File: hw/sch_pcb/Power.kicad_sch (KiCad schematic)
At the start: 20 parts, among them U1 NCP1117ST33, U11 TPS563249

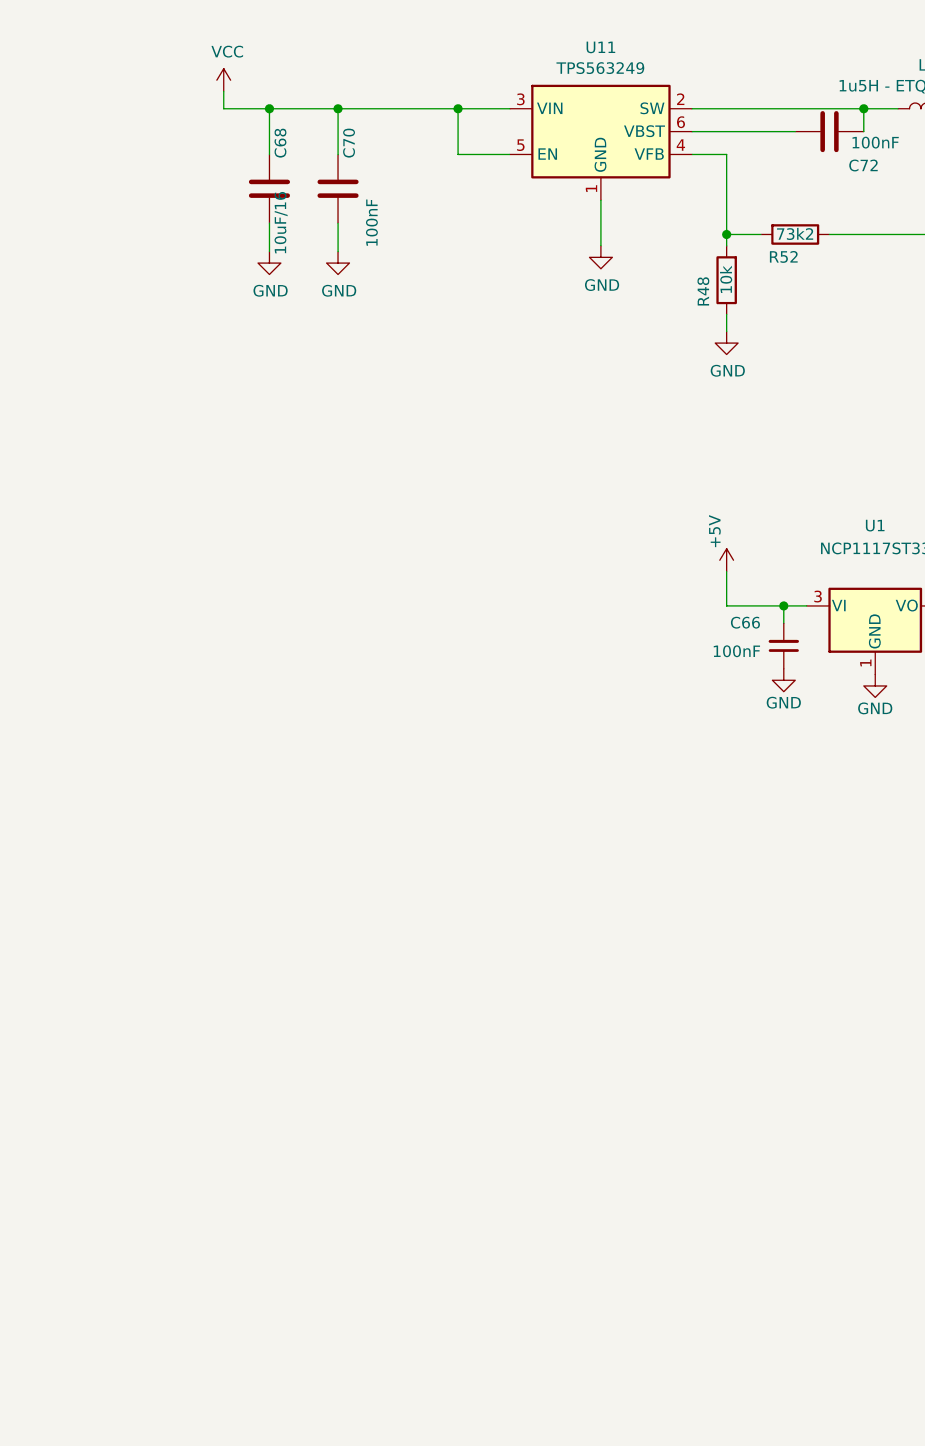
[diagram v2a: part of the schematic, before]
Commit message: Add thermistor #22, align text labels
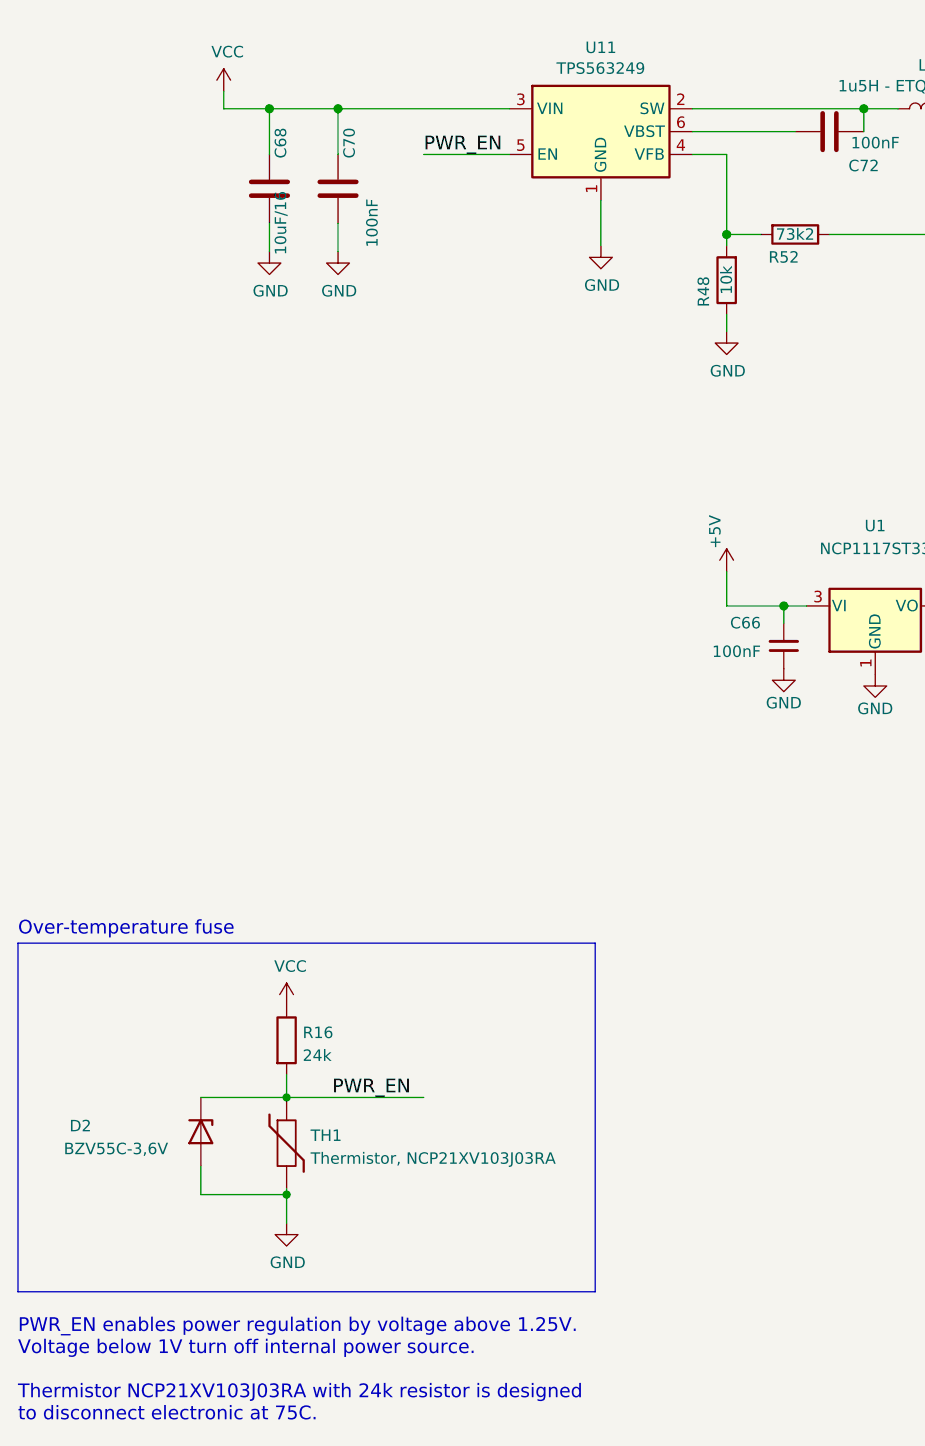
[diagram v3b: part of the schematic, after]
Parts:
- added D2: BZV55C-3,6V, Diode_SMD:D_MiniMELF, symbol Device:D_Zener
- added R16: 24k, Resistor_SMD:R_0805_2012Metric, symbol Device:R
- added TH1: Thermistor, NCP21XV103J03RA, Resistor_SMD:R_0805_2012Metric, symbol Device:Thermistor
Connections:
- net GND: now also D2.2 (A), TH1.2
- net VCC: now also R16.1; no longer U11.5 (EN)
- new net PWR_EN: D2.1 (K), R16.2, TH1.1, U11.5 (EN)
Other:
- note added: "Over-temperature fuse"
- note added: "PWR_EN enables power regulation by voltage above 1.25V. Voltage below 1V turn off internal power source. Thermistor NCP21XV103J03RA with 24k resistor is designed to disconnect electronic at 75C."
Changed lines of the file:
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@@
   (junction (at 83.185 31.75) (diameter 1.016) (color 0 0 0 0)
   )
+  (junction (at 77.47 141.605) (diameter 0) (color 0 0 0 0)
+  )
   (junction (at 160.02 86.995) (diameter 1.016) (color 0 0 0 0)
   )
@@
   (junction (at 132.715 86.995) (diameter 1.016) (color 0 0 0 0)
   )
-  (junction (at 96.52 31.75) (diameter 1.016) (color 0 0 0 0)
+  (junction (at 77.47 152.4) (diameter 0) (color 0 0 0 0)
   )
   (junction (at 207.645 31.75) (diameter 1.016) (color 0 0 0 0)
@@
   (junction (at 155.575 31.75) (diameter 1.016) (color 0 0 0 0)
   )
+  (polyline (pts (xy 47.625 124.46) (xy 111.76 124.46))
+    (stroke (width 0) (type default) (color 0 0 0 0))
+  )
+  (wire (pts (xy 77.47 139.065) (xy 77.47 141.605))
+    (stroke (width 0) (type default) (color 0 0 0 0))
+  )
   (wire (pts (xy 153.035 86.995) (xy 160.02 86.995))
     (stroke (width 0) (type solid) (color 0 0 0 0))
@@
     (stroke (width 0) (type solid) (color 0 0 0 0))
   )
+  (wire (pts (xy 77.47 155.575) (xy 77.47 152.4))
+    (stroke (width 0) (type default) (color 0 0 0 0))
+  )
   (wire (pts (xy 198.12 40.64) (xy 198.12 55.88))
     (stroke (width 0) (type solid) (color 0 0 0 0))
@@
     (stroke (width 0) (type solid) (color 0 0 0 0))
   )
+  (wire (pts (xy 77.47 141.605) (xy 92.71 141.605))
+    (stroke (width 0) (type default) (color 0 0 0 0))
+  )
   (wire (pts (xy 183.515 31.75) (xy 187.325 31.75))
     (stroke (width 0) (type solid) (color 0 0 0 0))
@@
     (stroke (width 0) (type solid) (color 0 0 0 0))
   )
-  (wire (pts (xy 96.52 31.75) (xy 96.52 36.83))
-    (stroke (width 0) (type solid) (color 0 0 0 0))
-  )
   (wire (pts (xy 183.515 45.72) (xy 183.515 31.75))
     (stroke (width 0) (type solid) (color 0 0 0 0))
@@
     (stroke (width 0) (type solid) (color 0 0 0 0))
   )
+  (polyline (pts (xy 47.625 124.46) (xy 47.625 163.195))
+    (stroke (width 0) (type default) (color 0 0 0 0))
+  )
   (wire (pts (xy 75.565 44.45) (xy 75.565 47.625))
     (stroke (width 0) (type solid) (color 0 0 0 0))
@@
     (stroke (width 0) (type solid) (color 0 0 0 0))
   )
-  (wire (pts (xy 102.235 36.83) (xy 96.52 36.83))
-    (stroke (width 0) (type solid) (color 0 0 0 0))
+  (wire (pts (xy 67.945 141.605) (xy 77.47 141.605))
+    (stroke (width 0) (type default) (color 0 0 0 0))
+  )
+  (wire (pts (xy 92.71 36.83) (xy 102.235 36.83))
+    (stroke (width 0) (type solid) (color 0 0 0 0))
+  )
+  (wire (pts (xy 67.945 149.225) (xy 67.945 152.4))
+    (stroke (width 0) (type default) (color 0 0 0 0))
   )
   (wire (pts (xy 194.945 31.75) (xy 198.12 31.75))
@@
     (stroke (width 0) (type solid) (color 0 0 0 0))
   )
-  (wire (pts (xy 102.235 31.75) (xy 96.52 31.75))
+  (polyline (pts (xy 111.76 163.195) (xy 47.625 163.195))
+    (stroke (width 0) (type default) (color 0 0 0 0))
+  )
+  (wire (pts (xy 83.185 31.75) (xy 102.235 31.75))
     (stroke (width 0) (type solid) (color 0 0 0 0))
   )
@@
     (stroke (width 0) (type solid) (color 0 0 0 0))
   )
+  (wire (pts (xy 67.945 152.4) (xy 77.47 152.4))
+    (stroke (width 0) (type default) (color 0 0 0 0))
+  )
   (wire (pts (xy 150.495 86.995) (xy 153.035 86.995))
     (stroke (width 0) (type solid) (color 0 0 0 0))
@@
     (stroke (width 0) (type solid) (color 0 0 0 0))
   )
+  (wire (pts (xy 77.47 152.4) (xy 77.47 151.765))
+    (stroke (width 0) (type default) (color 0 0 0 0))
+  )
   (wire (pts (xy 126.365 36.83) (xy 126.365 45.72))
     (stroke (width 0) (type solid) (color 0 0 0 0))
@@
     (stroke (width 0) (type solid) (color 0 0 0 0))
   )
+  (polyline (pts (xy 111.76 124.46) (xy 111.76 163.195))
+    (stroke (width 0) (type default) (color 0 0 0 0))
+  )
   (wire (pts (xy 70.485 29.845) (xy 70.485 31.75))
     (stroke (width 0) (type solid) (color 0 0 0 0))
@@
     (stroke (width 0) (type solid) (color 0 0 0 0))
   )
-  (wire (pts (xy 96.52 31.75) (xy 83.185 31.75))
-    (stroke (width 0) (type solid) (color 0 0 0 0))
-  )
   (wire (pts (xy 126.365 54.61) (xy 126.365 56.515))
     (stroke (width 0) (type solid) (color 0 0 0 0))
@@
     (stroke (width 0) (type solid) (color 0 0 0 0))
   )
+  (text "PWR_EN enables power regulation by voltage above 1.25V.\nVoltage below 1V turn off internal power source. \n\nThermistor NCP21XV103J03RA with 24k resistor is designed\nto disconnect electronic at 75C."
+    (at 47.625 177.8 0)
+    (effects (font (size 1.524 1.524)) (justify left bottom))
+  )
+  (text "Over-temperature fuse" (at 47.625 123.825 0)
+    (effects (font (size 1.524 1.524)) (justify left bottom))
+  )
+  (label "PWR_EN" (at 82.55 141.605 0)
+    (effects (font (size 1.524 1.524)) (justify left bottom))
+  )
   (label "3V3VO" (at 153.035 86.995 0)
+    (effects (font (size 1.524 1.524)) (justify left bottom))
+  )
+  (label "PWR_EN" (at 92.71 36.83 0)
     (effects (font (size 1.524 1.524)) (justify left bottom))
   )
@@
     (pin "2")
   )
+  (symbol (lib_id "Device:D_Zener") (at 67.945 145.415 270) (unit 1)
+    (in_bom yes) (on_board yes)
+    (property "Reference" "D2" (id 0) (at 53.34 144.78 90)
+      (effects (font (size 1.27 1.27)) (justify left))
+    )
+    (property "Value" "BZV55C-3,6V" (id 1) (at 52.705 147.32 90)
+      (effects (font (size 1.27 1.27)) (justify left))
+    )
+    (property "Footprint" "Diode_SMD:D_MiniMELF" (id 2) (at 67.945 145.415 0)
+      (effects (font (size 1.27 1.27)) hide)
+    )
+    (property "Datasheet" "~" (id 3) (at 67.945 145.415 0)
+      (effects (font (size 1.27 1.27)) hide)
+    )
+    (pin "1")
+    (pin "2")
+  )
   (symbol (lib_id "power:+5V") (at 216.535 27.305 0) (unit 1)
     (in_bom yes) (on_board yes)
@@
     (pin "1")
   )
+  (symbol (lib_id "power:VCC") (at 77.47 131.445 0) (unit 1)
+    (in_bom yes) (on_board yes)
+    (property "Reference" "#PWR024" (id 0) (at 77.47 135.255 0)
+      (effects (font (size 1.27 1.27)) hide)
+    )
+    (property "Value" "VCC" (id 1) (at 77.9018 127.0508 0))
+    (property "Footprint" "" (id 2) (at 77.47 131.445 0)
+      (effects (font (size 1.27 1.27)) hide)
+    )
+    (property "Datasheet" "" (id 3) (at 77.47 131.445 0)
+      (effects (font (size 1.27 1.27)) hide)
+    )
+    (pin "1")
+  )
   (symbol (lib_id "QFHMIX01C-rescue:L-device-QFHMIX01B-rescue") (at 167.64 86.995 90) (unit 1)
     (in_bom yes) (on_board yes)
@@
     )
     (pin "1")
+  )
+  (symbol (lib_id "Device:Thermistor") (at 77.47 146.685 0) (unit 1)
+    (in_bom yes) (on_board yes) (fields_autoplaced)
+    (property "Reference" "TH1" (id 0) (at 80.137 145.8503 0)
+      (effects (font (size 1.27 1.27)) (justify left))
+    )
+    (property "Value" "Thermistor, NCP21XV103J03RA" (id 1) (at 80.137 148.3872 0)
+      (effects (font (size 1.27 1.27)) (justify left))
+    )
+    (property "Footprint" "Resistor_SMD:R_0805_2012Metric" (id 2) (at 77.47 146.685 0)
+      (effects (font (size 1.27 1.27)) hide)
+    )
+    (property "Datasheet" "https://www.murata.com/~/media/webrenewal/support/library/catalog/products/thermistor/ntc/r44e.ashx?la=en-us" (id 3) (at 77.47 146.685 0)
+      (effects (font (size 1.27 1.27)) hide)
+    )
+    (pin "1")
+    (pin "2")
   )
   (symbol (lib_id "Device:C") (at 155.575 37.465 180) (unit 1)
@@
     (pin "2")
   )
+  (symbol (lib_id "Device:R") (at 77.47 135.255 0) (unit 1)
+    (in_bom yes) (on_board yes) (fields_autoplaced)
+    (property "Reference" "R16" (id 0) (at 79.248 134.4203 0)
+      (effects (font (size 1.27 1.27)) (justify left))
+    )
+    (property "Value" "24k" (id 1) (at 79.248 136.9572 0)
+      (effects (font (size 1.27 1.27)) (justify left))
+    )
+    (property "Footprint" "Resistor_SMD:R_0805_2012Metric" (id 2) (at 75.692 135.255 90)
+      (effects (font (size 1.27 1.27)) hide)
+    )
+    (property "Datasheet" "~" (id 3) (at 77.47 135.255 0)
+      (effects (font (size 1.27 1.27)) hide)
+    )
+    (pin "1")
+    (pin "2")
+  )
   (symbol (lib_id "Device:R") (at 216.535 41.91 0) (unit 1)
     (in_bom yes) (on_board yes)
@@
       (effects (font (size 1.27 1.27)) hide)
     )
+    (pin "1")
+  )
+  (symbol (lib_id "power:GND") (at 77.47 155.575 0) (unit 1)
+    (in_bom yes) (on_board yes)
+    (property "Reference" "#PWR025" (id 0) (at 77.47 161.925 0)
+      (effects (font (size 1.27 1.27)) hide)
+    )
+    (property "Value" "GND" (id 1) (at 77.597 159.9692 0))
+    (property "Footprint" "" (id 2) (at 77.47 155.575 0)
+      (effects (font (size 1.27 1.27)) hide)
+    )
+    (property "Datasheet" "" (id 3) (at 77.47 155.575 0)
+      (effects (font (size 1.27 1.27)) hide)
+    )
